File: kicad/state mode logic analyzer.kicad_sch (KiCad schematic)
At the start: 131 parts, among them J1 USB0, J2 Exp Out, J5 Exp In, J6 Probe, J7 SWD0, J8 Probe Power, J9 5V USB0, SW1 Reset 0, SW2 Boot 0, U1 RP2040, U10 74LVC245APW, U11 74LVC245APW, U3 74HC4520D, U4 LTC6994xS6-1, U5 MCP4725, U6 AD5241BRZ1M, U7 IS25LP128F-JBLE, U9 MCP1826S, Y1 ECS-120-18-33-JEM-TR

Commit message: added distributor part numbers
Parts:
- D7: SPN (none) -> 37K9805; STANDARD (none) -> 37K9805
- J2: SPN (none) -> 98K4897
- J5: SPN (none) -> 82p5246
- J6: SPN (none) -> 20X0993
- J7: SPN (none) -> 01R3466; STANDARD Manufacturer Recommendation -> 01R3466
- SW1, SW2: SPN (none) -> 35AH5296
- TP0, TP1, TP10, TP100, TP101, TP102, TP103, TP104, TP105, TP106, TP107, TP108, TP109, TP11, TP110, TP111, TP112, TP113, TP114, TP115, TP12, TP13, TP133, TP14, TP15, TP16, TP17, TP18, TP19, TP2, TP3, TP4, TP5, TP6, TP7, TP8, TP9: SPN (none) -> 75R5336
- U3: SPN (none) -> 74AH2471
- U4: SPN (none) -> 50AK4110; STANDARD (none) -> 50AK4110
- U5: SPN (none) -> 08N6516
- U9: SPN (none) -> 08N6493
- Y1: SPN (none) -> 26AJ5824

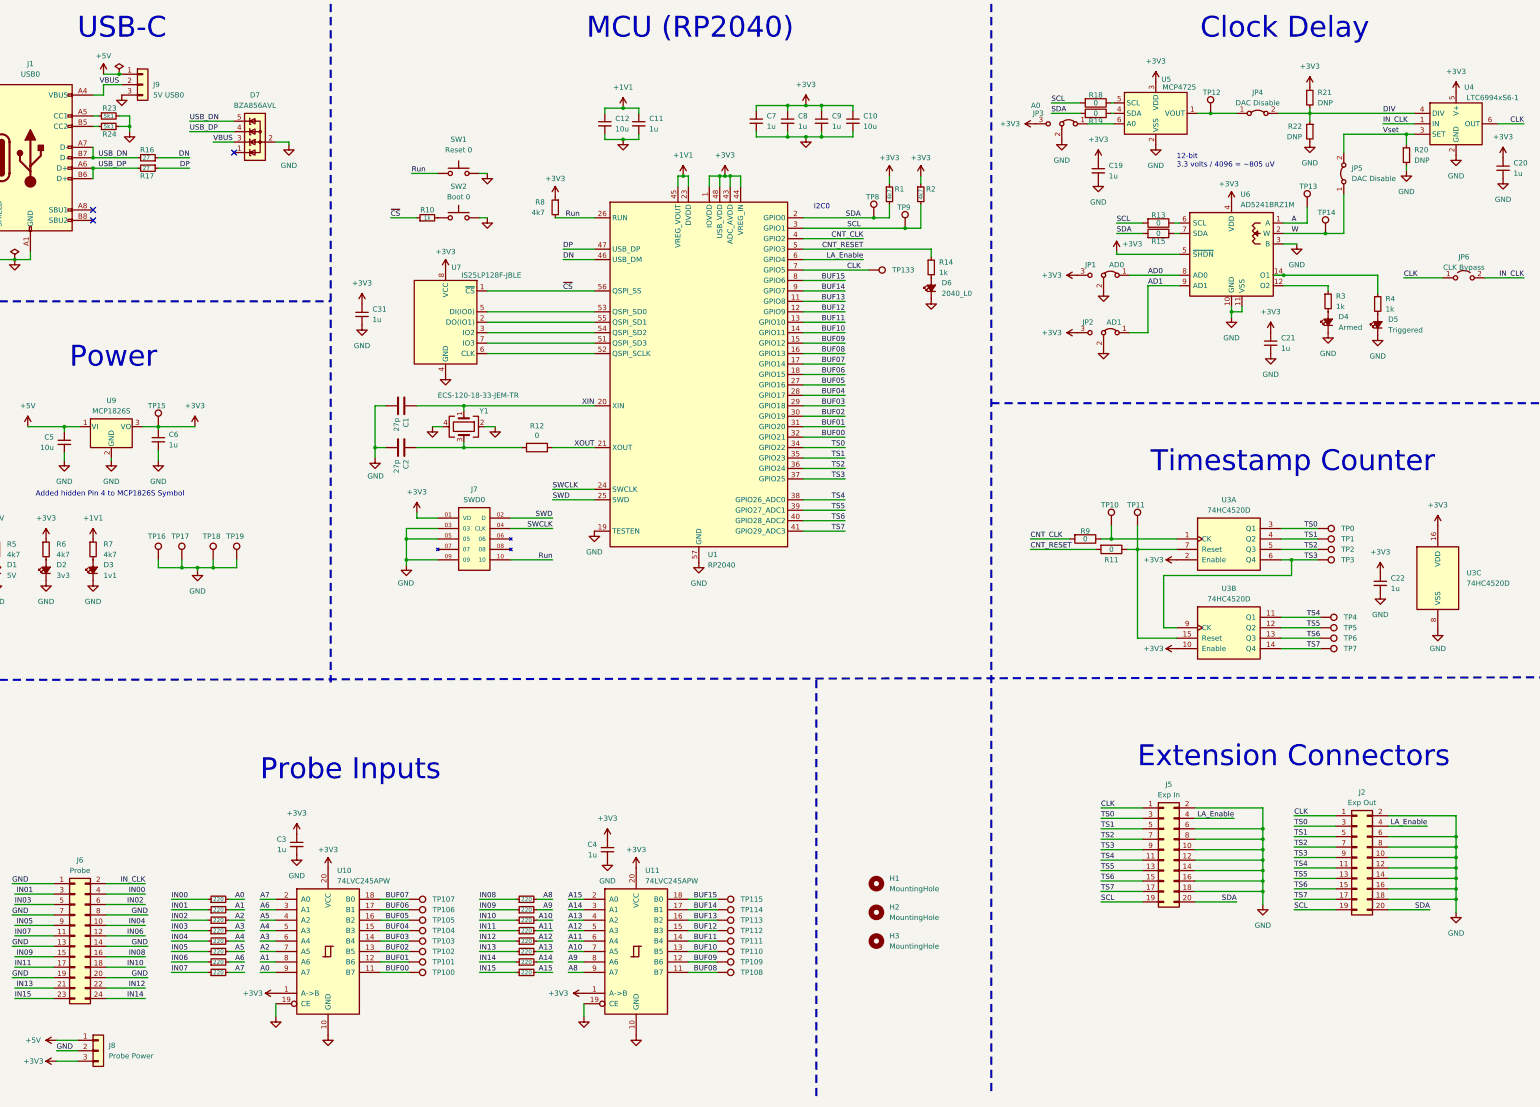
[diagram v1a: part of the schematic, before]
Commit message: fixed J desgs and swapped prog header part num
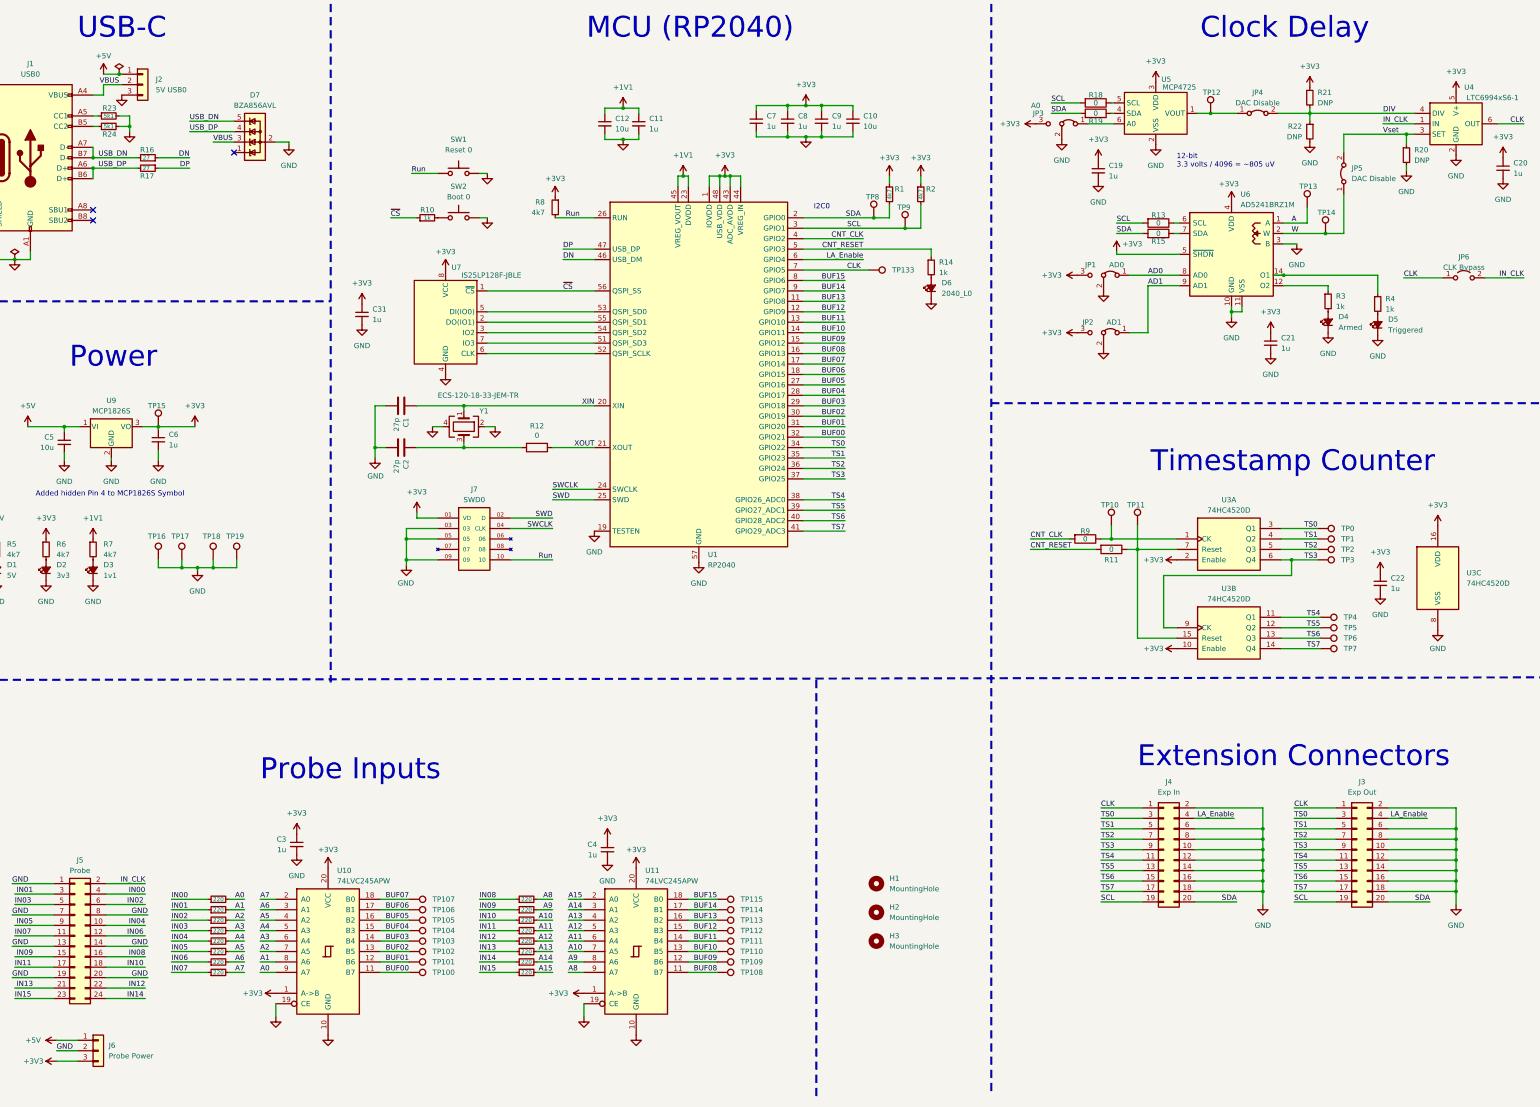
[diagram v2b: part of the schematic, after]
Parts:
- J4: renamed from J5; SPN 82p5246 -> 47ac7181
- J7: Amp SPN (none) -> 83AH7573; Note (none) -> I'm trying an alternate part; SPN 01R3466 -> (none); Samtec SPN (none) -> 01R3466
- U1: SPN (none) -> 49AJ8739
- renumbered J9 to J2, J2 to J3, J6 to J5, J8 to J6
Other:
- moved on the sheet: J3
